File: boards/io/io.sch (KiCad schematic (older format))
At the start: 13 parts, among them J1 CU, J2 KB_ROW, J3 KB_COL, U1 74ACT32, U2 74ACT08, U3 74ACT00, U4 AT28C256-PLCC32, U5 62256-TSOP, U6 RC1602A, U7 74ACT273, U8 74HC244

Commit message: IO board footprint assignments
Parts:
- added C1, C2, C3, C4, C5, C6: 0.1u, Capacitor_SMD:C_0805_2012Metric, symbol Device:C
- added C7: 25.0x6.3v, Capacitor_SMD:CP_Elec_4x4.5, symbol Device:CP
- added D1, D2, D3, D4, D5: LED, LED_SMD:LED_0805_2012Metric, symbol Device:LED
- added H1, H2, H3, H4: MountingHole, MountingHole:MountingHole_3.2mm_M3, symbol Mechanical:MountingHole
- added R10, R11, R12, R13, R14, R7, R8, R9: 10k, Resistor_SMD:R_0805_2012Metric, symbol Device:R
- added R2, R3, R4, R5, R6: LED, Resistor_SMD:R_0805_2012Metric, symbol Device:R
- J1: footprint Connector_PinSocket_2.54mm:PinSocket_2x20_P2.54mm_Horizontal -> Connector_PinHeader_2.54mm:PinHeader_2x20_P2.54mm_Horizontal
- J2, J3: footprint (none) -> Connector_PinHeader_2.54mm:PinHeader_1x08_P2.54mm_Vertical
- R1: footprint (none) -> Resistor_SMD:R_0805_2012Metric
- RV1: footprint (none) -> Potentiometer_THT:Potentiometer_Bourns_3296Z_Horizontal
- U1, U2, U3: footprint (none) -> Package_SO:TSSOP-14_4.4x5mm_P0.65mm
- U4: footprint (none) -> missing:PLCC-32_SMD_Socket
- U6: footprint Display:RC1602A -> Connector_PinSocket_2.54mm:PinSocket_1x16_P2.54mm_Vertical
- U7: value 74ACT273 -> 74AC273; footprint (none) -> Package_SO:TSSOP-20_4.4x6.5mm_P0.65mm
- U8: value 74HC244 -> 74ACT244; footprint (none) -> Package_SO:TSSOP-20_4.4x6.5mm_P0.65mm
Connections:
- net GND: now also C1.2, C2.2, C3.2, C4.2, C5.2, C6.2, C7.2
- net VCC: now also C1.1, C2.1, C3.1, C4.1, C5.1, C6.1, C7.1, R2.1, R3.1, R4.1, R5.1, R6.1
- net a15: now also D4.1 (K)
- net ~io_cs: now also D5.1 (K)
- net ~oe: now also D2.1 (K)
- net ~ram_cs: now also D3.1 (K)
- net ~we: now also D1.1 (K)
- net at U7.12 (Q4): now also R11.2; no longer J2.5 (Pin_5)
- net at U7.15 (Q5): now also R12.2; no longer J2.6 (Pin_6)
- net at U7.16 (Q6): now also R13.2; no longer J2.7 (Pin_7)
- net at U7.19 (Q7): now also R14.2; no longer J2.8 (Pin_8)
- net at U7.2 (Q0): now also R7.2; no longer J2.1 (Pin_1)
- net at U7.5 (Q1): now also R8.2; no longer J2.2 (Pin_2)
- net at U7.6 (Q2): now also R9.2; no longer J2.3 (Pin_3)
- net at U7.9 (Q3): now also R10.2; no longer J2.4 (Pin_4)
- new net: J2.1 (Pin_1), R7.1
- new net: J2.2 (Pin_2), R8.1
- new net: J2.3 (Pin_3), R9.1
- new net: J2.4 (Pin_4), R10.1
- new net: J2.5 (Pin_5), R11.1
- new net: J2.6 (Pin_6), R12.1
- new net: J2.7 (Pin_7), R13.1
- new net: J2.8 (Pin_8), R14.1
- new net: D1.2 (A), R2.2
- new net: D2.2 (A), R3.2
- new net: D3.2 (A), R4.2
- new net: D4.2 (A), R5.2
- new net: D5.2 (A), R6.2
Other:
- note added: "F000 Keyboard\nF002 LCD control\nF003 LCD data"
- note removed: "F000 LCD control\nF001 LCD data"
- moved on the sheet: J2, J3, U8

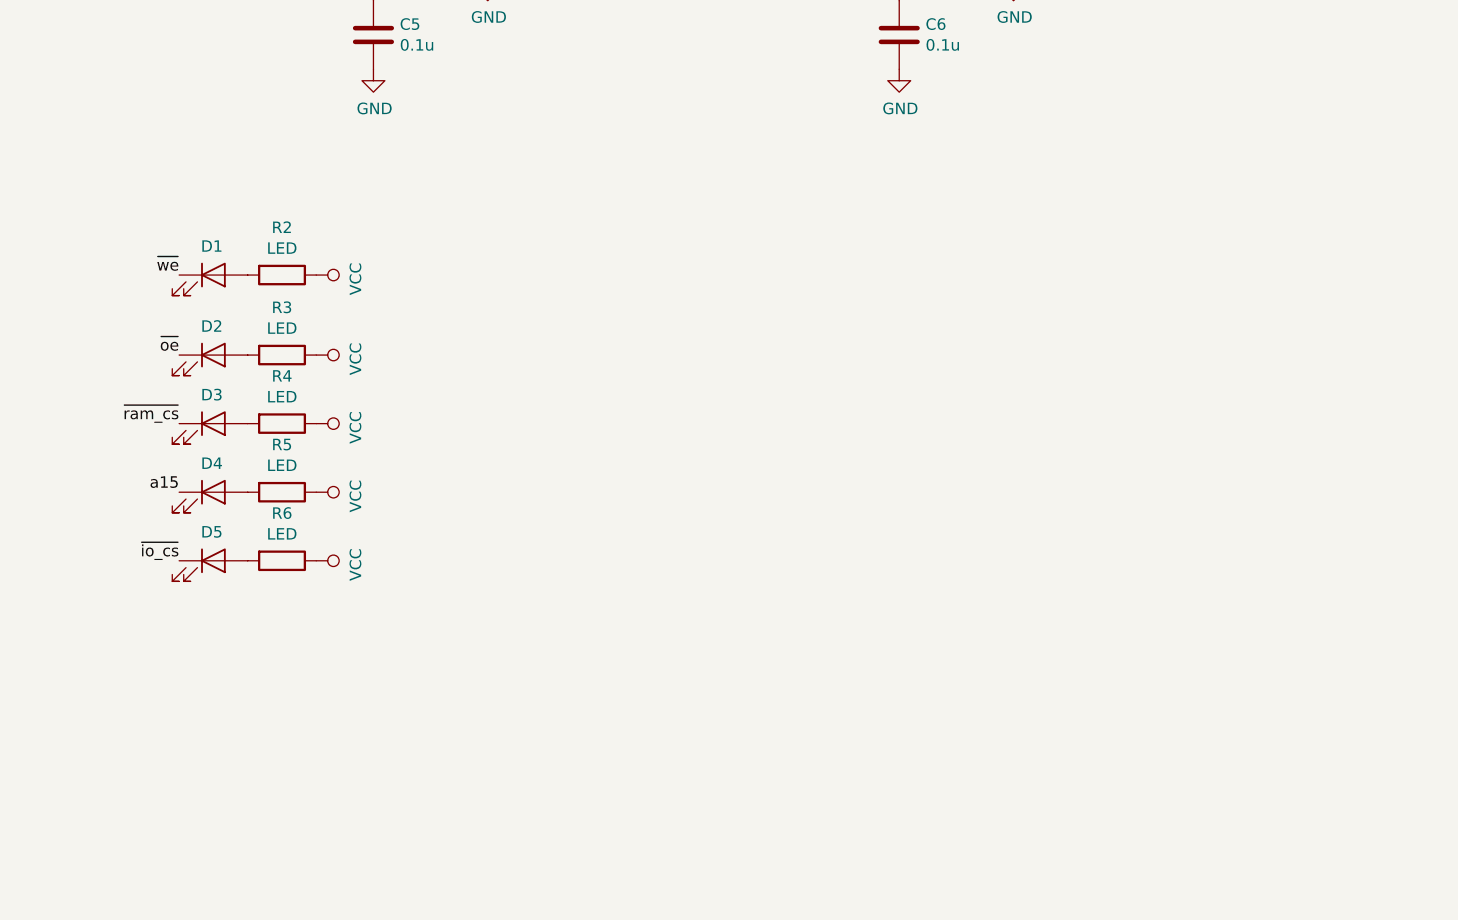
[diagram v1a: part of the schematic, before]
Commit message: IO board: A and D LEDs
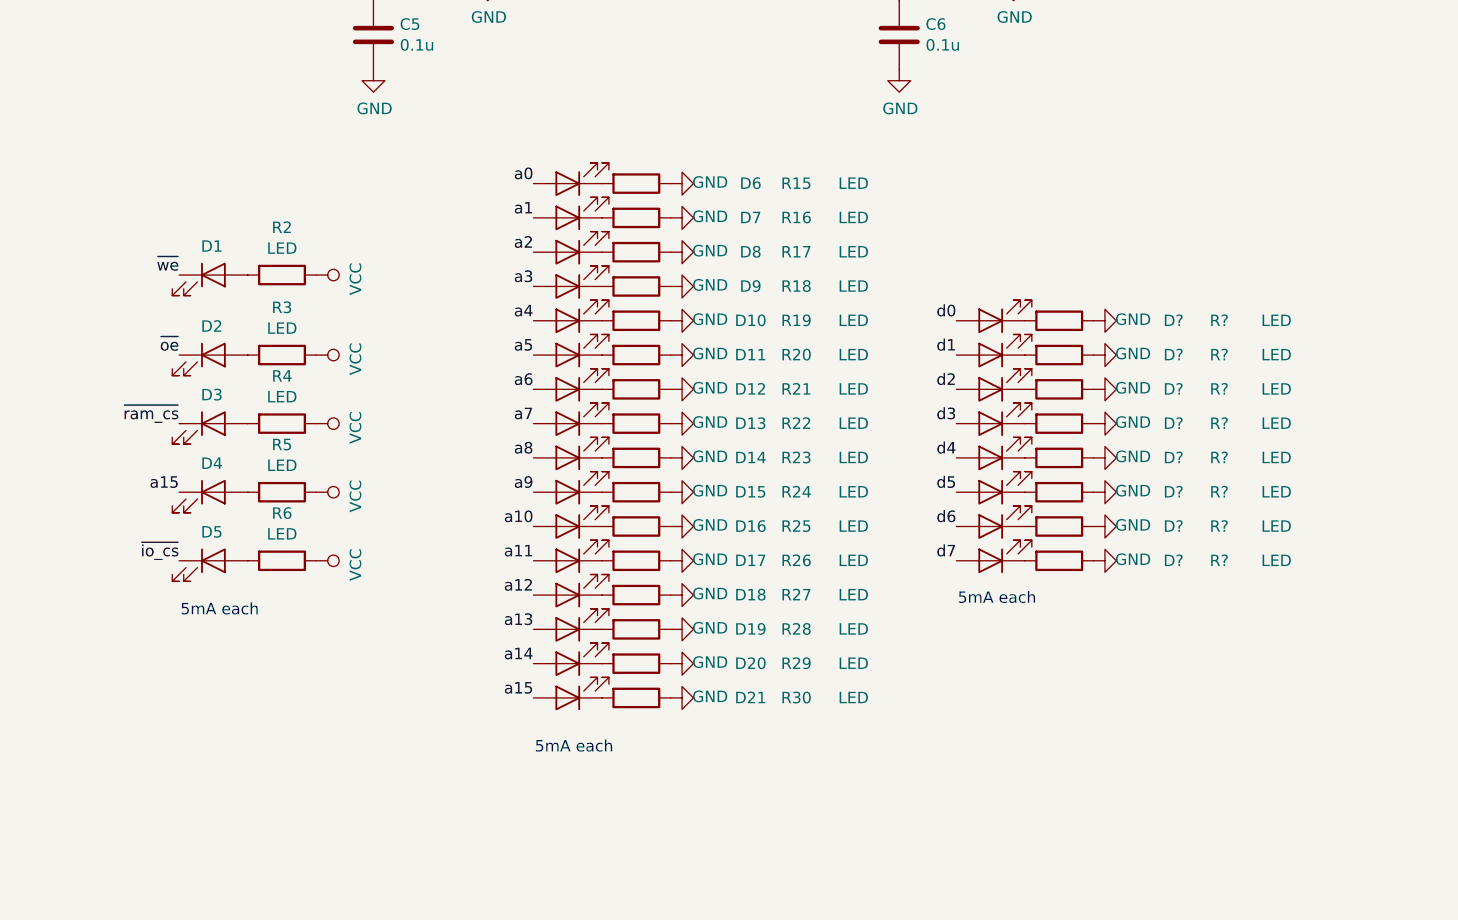
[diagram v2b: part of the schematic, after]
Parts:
- added D10, D11, D12, D13, D14, D15, D16, D17, D18, D19, D20, D21, D6, D7, D8, D9, D? (x8): LED, LED_SMD:LED_0805_2012Metric, symbol Device:LED
- added R15, R16, R17, R18, R19, R20, R21, R22, R23, R24, R25, R26, R27, R28, R29, R30, R? (x8): LED, Resistor_SMD:R_0805_2012Metric, symbol Device:R
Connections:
- net GND: now also R15.1, R16.1, R17.1, R18.1, R19.1, R20.1, R21.1, R22.1, R23.1, R24.1, R25.1, R26.1, R27.1, R28.1, R29.1, R30.1, R?.1, R?.1, R?.1, R?.1, R?.1, R?.1, R?.1, R?.1
- net a0: now also D6.2 (A)
- net a1: now also D7.2 (A)
- net a10: now also D16.2 (A)
- net a11: now also D17.2 (A)
- net a12: now also D18.2 (A)
- net a13: now also D19.2 (A)
- net a14: now also D20.2 (A)
- net a15: now also D21.2 (A)
- net a2: now also D8.2 (A)
- net a3: now also D9.2 (A)
- net a4: now also D10.2 (A)
- net a5: now also D11.2 (A)
- net a6: now also D12.2 (A)
- net a7: now also D13.2 (A)
- net a8: now also D14.2 (A)
- net a9: now also D15.2 (A)
- net d0: now also D?.2 (A)
- net d1: now also D?.2 (A)
- net d2: now also D?.2 (A)
- net d3: now also D?.2 (A)
- net d4: now also D?.2 (A)
- net d5: now also D?.2 (A)
- net d6: now also D?.2 (A)
- net d7: now also D?.2 (A)
- new net: D6.1 (K), R15.2
- new net: D7.1 (K), R16.2
- new net: D8.1 (K), R17.2
- new net: D9.1 (K), R18.2
- new net: D10.1 (K), R19.2
- new net: D11.1 (K), R20.2
- new net: D12.1 (K), R21.2
- new net: D13.1 (K), R22.2
- new net: D14.1 (K), R23.2
- new net: D15.1 (K), R24.2
- new net: D16.1 (K), R25.2
- new net: D17.1 (K), R26.2
- new net: D18.1 (K), R27.2
- new net: D19.1 (K), R28.2
- new net: D20.1 (K), R29.2
- new net: D21.1 (K), R30.2
- new net: D?.1 (K), R?.2 (x8)
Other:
- note added: "5mA each"

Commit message: IO board
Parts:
- added R39, R40, R41, R42, R43, R44, R45, R46: 10k, Resistor_SMD:R_0805_2012Metric, symbol Device:R
- R10, R11, R12, R13, R14, R7, R8, R9: value 10k -> 1k
- gave numbers to parts that had none: 16
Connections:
- net VCC: now also R39.2, R40.2, R41.2, R42.2, R43.2, R44.2, R45.2, R46.2
- net at J3.8 (Pin_8), U8.11 (2A3): now also R46.1
- net at J3.7 (Pin_7), U8.13 (2A2): now also R45.1
- net at J3.6 (Pin_6), U8.15 (2A1): now also R44.1
- net at J3.5 (Pin_5), U8.17 (2A0): now also R43.1
- net at J3.1 (Pin_1), U8.2 (1A0): now also R39.1
- net at J3.2 (Pin_2), U8.4 (1A1): now also R40.1
- net at J3.3 (Pin_3), U8.6 (1A2): now also R41.1
- net at J3.4 (Pin_4), U8.8 (1A3): now also R42.1
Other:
- moved on the sheet: C6, J3, U8

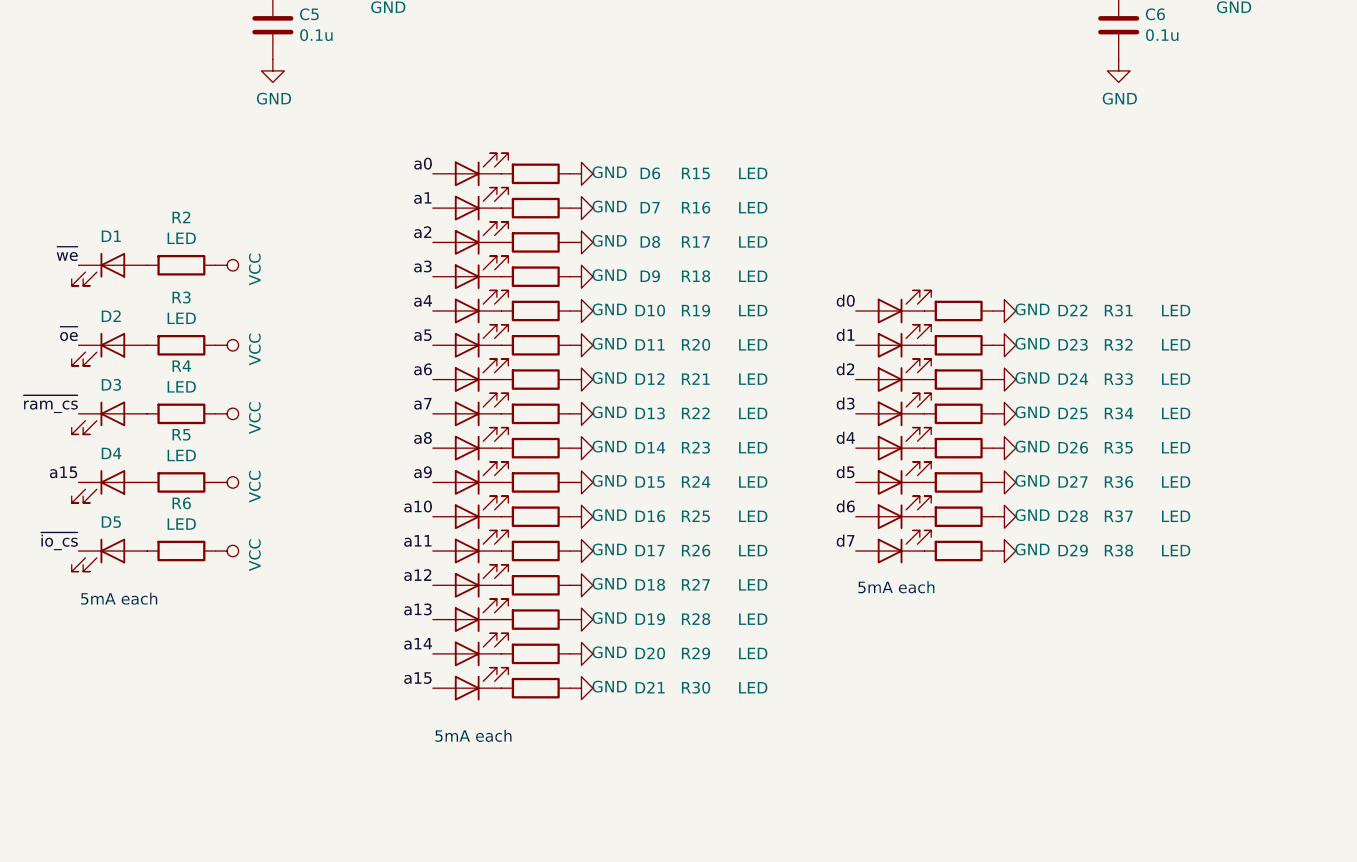
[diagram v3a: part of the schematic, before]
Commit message: LEDs and LED resistors
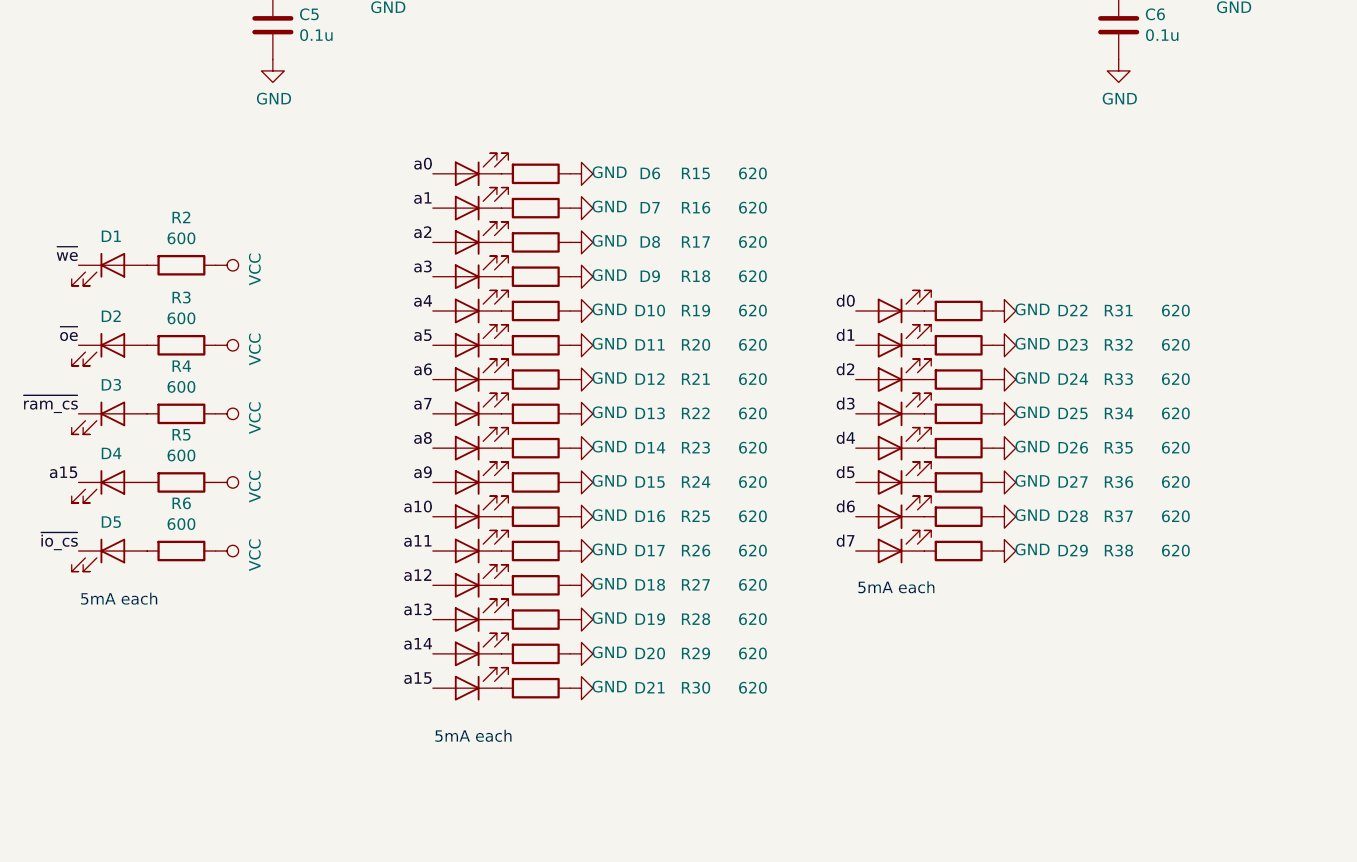
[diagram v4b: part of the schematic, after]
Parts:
- D1, D2, D3, D4, D5: value LED -> KP-2012CGCK
- D10, D11, D12, D13, D14, D15, D16, D17, D18, D19, D20, D21, D22, D23, D24, D25, D26, D27, D28, D29, D6, D7, D8, D9: value LED -> KP-2012EC
- R15, R16, R17, R18, R19, R20, R21, R22, R23, R24, R25, R26, R27, R28, R29, R30, R31, R32, R33, R34, R35, R36, R37, R38: value LED -> 620
- R2, R3, R4, R5, R6: value LED -> 600
